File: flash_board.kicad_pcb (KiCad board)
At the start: 2 copper layers, 62.9 x 45.1 mm, 9 parts, among them J1 Conn_02x16_Row_Letter_First, J2 Conn_02x03_Counter_Clockwise, U1 SST39SF040

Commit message: Updated board to hopefully final shape
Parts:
- moved C1 4.48 mm to (128.3, 111.1)
- moved J2 4.48 mm to (120.0, 101.6)
- moved JP1 4.48 mm to (127.0, 94.6)
- moved R3 4.48 mm to (120.0, 87.6)
- moved R4 4.48 mm to (120.0, 97.2)
- moved R1 4.48 mm to (123.2, 82.6)
- moved R2 4.48 mm to (123.2, 97.2)
- moved U1 4.48 mm to (147.4, 110.5)
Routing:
- net GND: track 165.2 -> 310.3 mm
- net +5V: track 149.6 -> 139.7 mm
- net /A14: track 84.4 -> 75.7 mm
- net /A1: track 41.8 -> 34.0 mm, vias 1 -> 0
- net /A13: track 76.7 -> 69.5 mm
- net /A3: track 40.8 -> 33.9 mm
- net /~{RD}: track 51.8 -> 45.1 mm
- net /A5: track 33.1 -> 26.4 mm
- net /~{WR}: track 64.2 -> 57.7 mm
- net /A11: track 48.9 -> 42.7 mm
- net /A15: track 56.6 -> 51.1 mm
- net /A10: track 58.4 -> 53.1 mm
- net /A6: track 36.6 -> 31.5 mm
- net /A8: track 47.9 -> 42.9 mm
- net /A9: track 49.0 -> 44.0 mm
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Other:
- board size 62.9 x 45.1 mm -> 57.9 x 45.7 mm

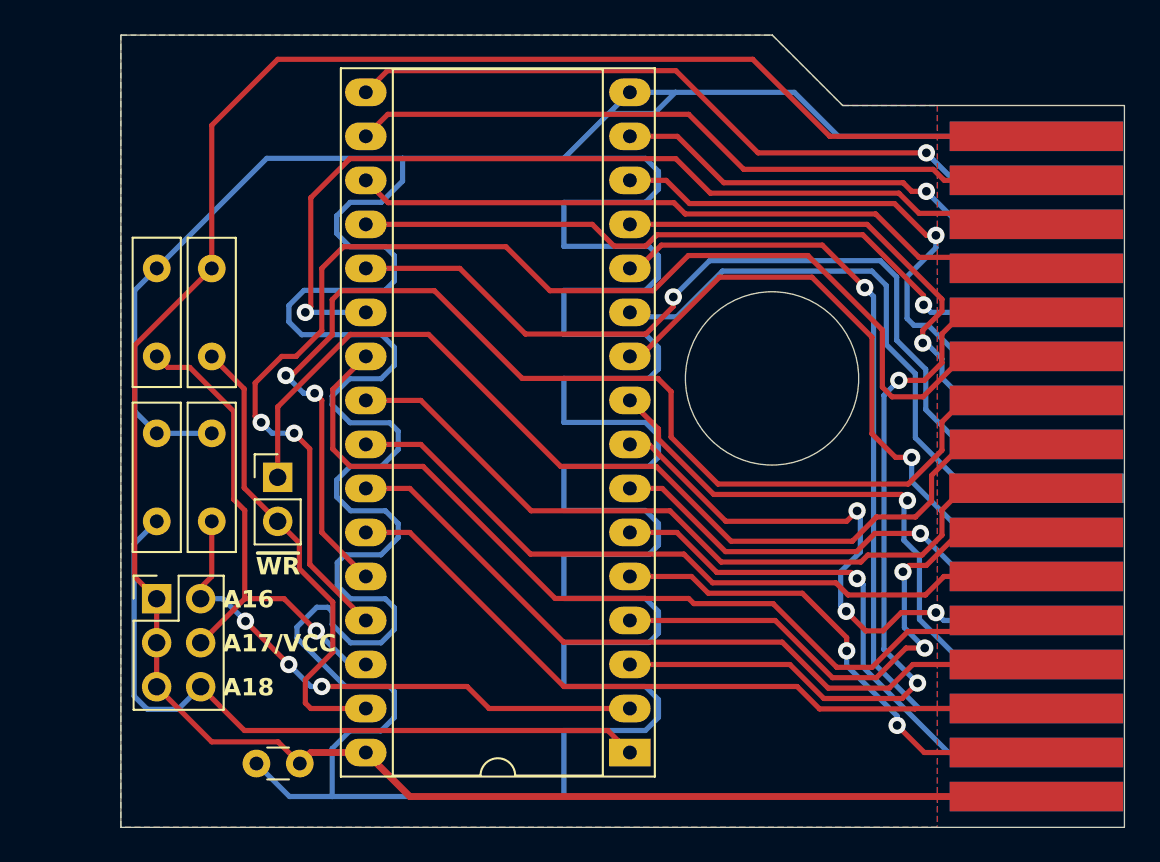
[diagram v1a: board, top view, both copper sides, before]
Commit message: Resized board to stay flush with case
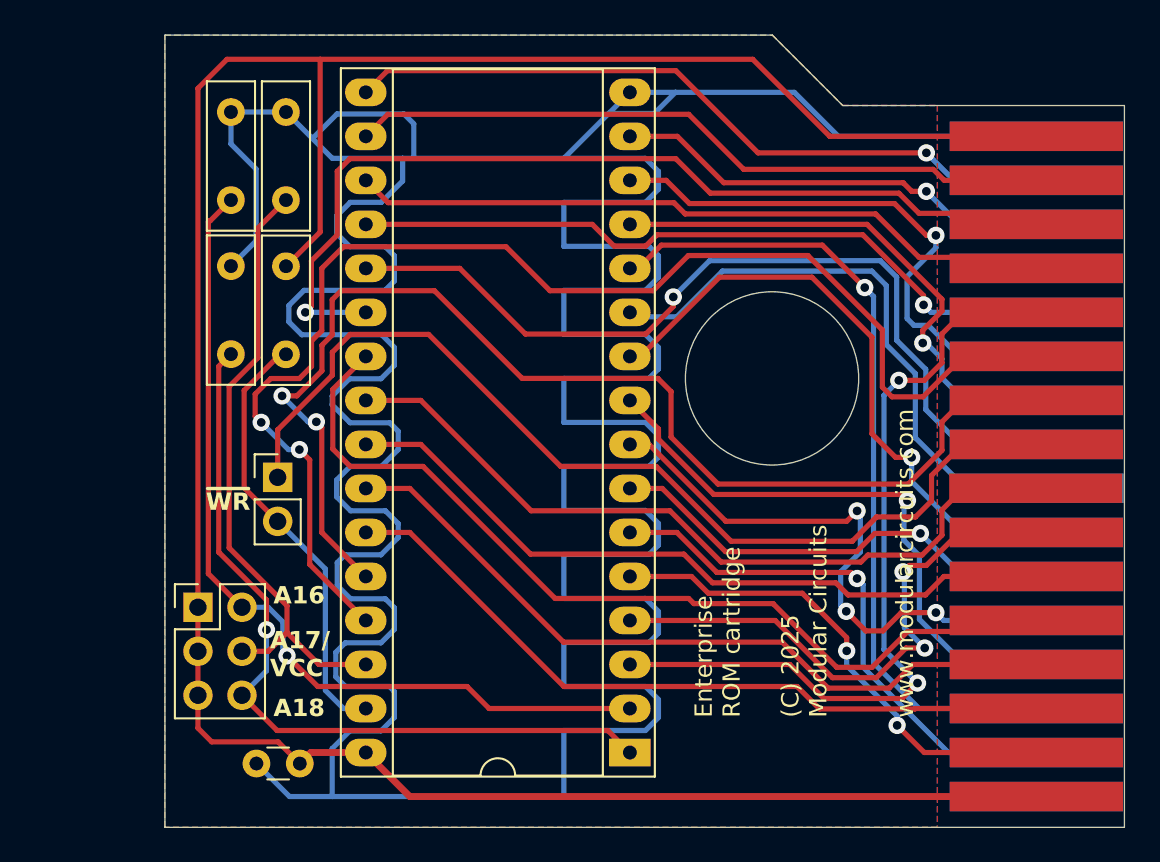
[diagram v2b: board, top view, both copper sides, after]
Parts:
- moved R2 18.6 mm to (124.3, 78.6)
- moved R3 11.7 mm to (127.5, 78.6)
- moved R4 10.6 mm to (124.3, 87.5)
- moved R1 4.28 mm to (127.5, 82.4)
- moved J2 2.43 mm to (122.4, 102.1)
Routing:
- net /A16: track 32.1 -> 50.9 mm, vias 3 -> 1
- net +5V: track 139.7 -> 151.2 mm
- net /A17: track 29.0 -> 36.1 mm, vias 1 -> 0
- net GND: track 310.3 -> 303.3 mm
- net /A18: track 41.7 -> 45.5 mm, vias 0 -> 1
- net /~{PGM}: track 27.2 -> 25.3 mm
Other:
- board size 57.9 x 45.7 mm -> 55.4 x 45.7 mm
- board text added: "(C) 2025 Modular Circuits"
- board text added: "A17/ VCC"
- board text added: "Enterprise ROM cartridge"
- board text added: "www.modularcircuits.com"
- board text removed: "A17/VCC"

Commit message: Some small fixes and release package.
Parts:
- J1: moved to F.Cu
- turned J1 to 0 degrees
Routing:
- net GND: track 303.3 -> 305.9 mm
